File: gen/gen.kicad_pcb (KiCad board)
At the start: 2 copper layers, 40.6 x 40.6 mm, 16 parts

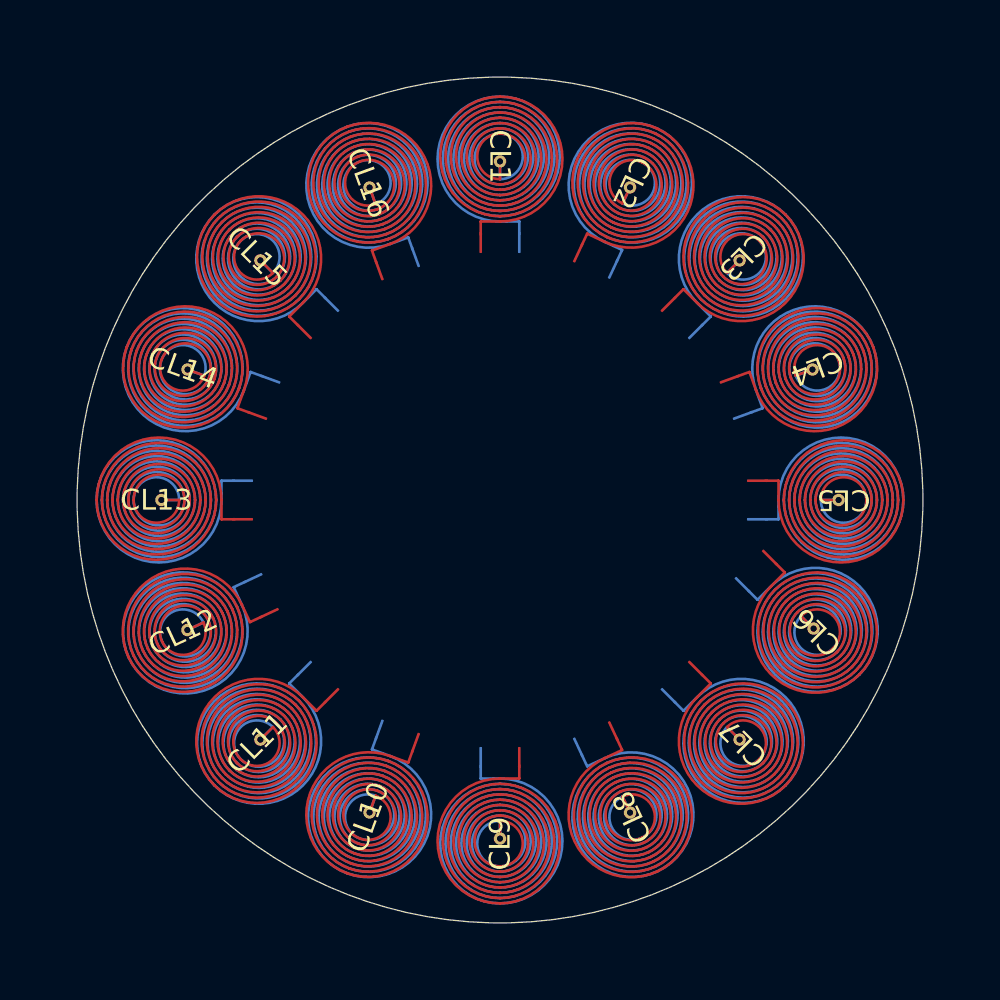
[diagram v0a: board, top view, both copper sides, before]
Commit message: Added 6 layer coils
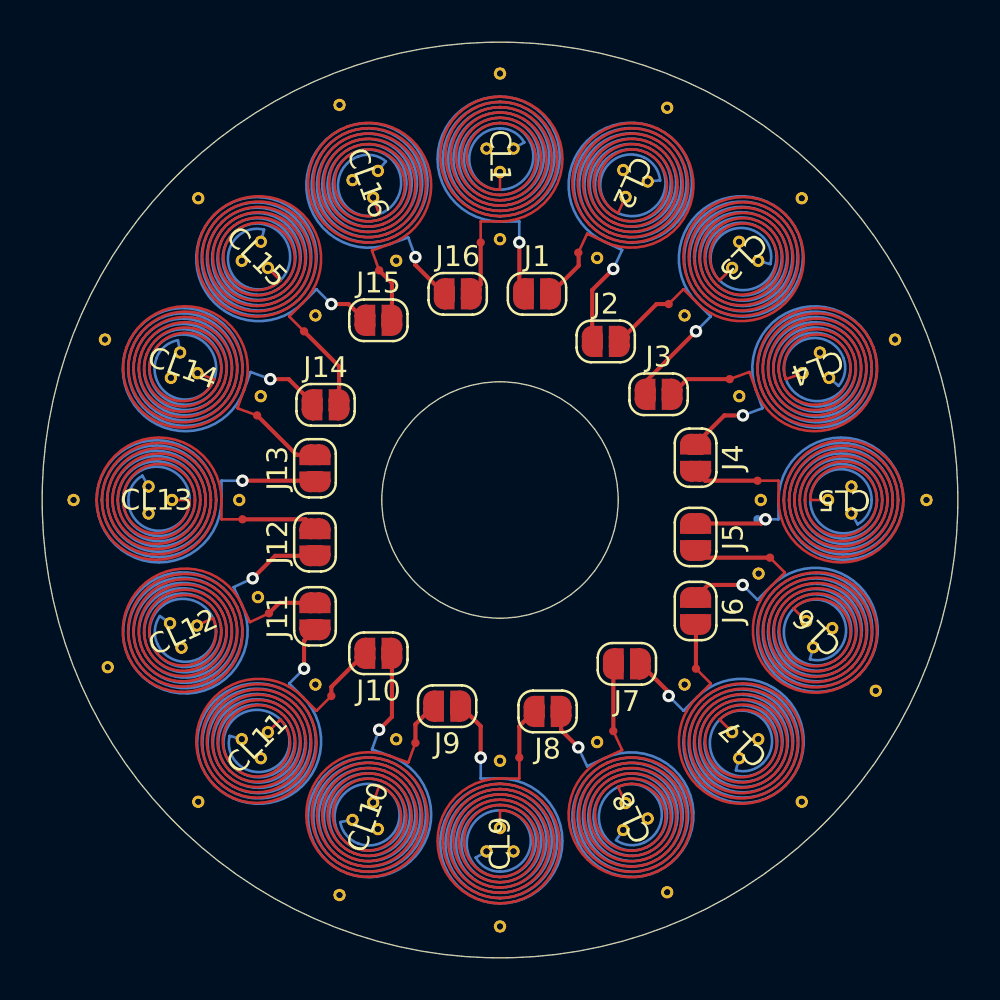
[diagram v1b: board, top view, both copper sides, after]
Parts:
- added J1: Conn_01x02_Pin, Jumper:SolderJumper-2_P1.3mm_Open_RoundedPad1.0x1.5mm, F.Cu at (154.2, 91.7)
- added J10: Conn_01x02_Pin, Jumper:SolderJumper-2_P1.3mm_Open_RoundedPad1.0x1.5mm, F.Cu at (146.6, 109.0)
- added J11: Conn_01x02_Pin, Jumper:SolderJumper-2_P1.3mm_Open_RoundedPad1.0x1.5mm, F.Cu at (143.5, 107.2)
- added J12: Conn_01x02_Pin, Jumper:SolderJumper-2_P1.3mm_Open_RoundedPad1.0x1.5mm, F.Cu at (143.5, 103.6)
- added J13: Conn_01x02_Pin, Jumper:SolderJumper-2_P1.3mm_Open_RoundedPad1.0x1.5mm, F.Cu at (143.5, 100.1)
- added J14: Conn_01x02_Pin, Jumper:SolderJumper-2_P1.3mm_Open_RoundedPad1.0x1.5mm, F.Cu at (144.0, 97.0)
- added J15: Conn_01x02_Pin, Jumper:SolderJumper-2_P1.3mm_Open_RoundedPad1.0x1.5mm, F.Cu at (146.6, 93.0)
- added J16: Conn_01x02_Pin, Jumper:SolderJumper-2_P1.3mm_Open_RoundedPad1.0x1.5mm, F.Cu at (150.4, 91.7)
- added J2: Conn_01x02_Pin, Jumper:SolderJumper-2_P1.3mm_Open_RoundedPad1.0x1.5mm, F.Cu at (157.5, 94.0)
- added J3: Conn_01x02_Pin, Jumper:SolderJumper-2_P1.3mm_Open_RoundedPad1.0x1.5mm, F.Cu at (160.0, 96.5)
- added J4: Conn_01x02_Pin, Jumper:SolderJumper-2_P1.3mm_Open_RoundedPad1.0x1.5mm, F.Cu at (161.8, 99.6)
- added J5: Conn_01x02_Pin, Jumper:SolderJumper-2_P1.3mm_Open_RoundedPad1.0x1.5mm, F.Cu at (161.8, 103.4)
- added J6: Conn_01x02_Pin, Jumper:SolderJumper-2_P1.3mm_Open_RoundedPad1.0x1.5mm, F.Cu at (161.8, 106.9)
- added J7: Conn_01x02_Pin, Jumper:SolderJumper-2_P1.3mm_Open_RoundedPad1.0x1.5mm, F.Cu at (158.5, 109.5)
- added J8: Conn_01x02_Pin, Jumper:SolderJumper-2_P1.3mm_Open_RoundedPad1.0x1.5mm, F.Cu at (154.7, 111.8)
- added J9: Conn_01x02_Pin, Jumper:SolderJumper-2_P1.3mm_Open_RoundedPad1.0x1.5mm, F.Cu at (149.9, 111.5)
- CL1, CL10, CL11, CL12, CL13, CL14, CL15, CL16, CL2, CL3, CL4, CL5, CL6, CL7, CL8, CL9: value SMALL_COIL -> L; footprint PCB Coils:SMALL_COIL -> PCB Coils:SMALL_COIL_6
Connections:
- CL1 pad 1: (no net) -> Net-(J16-Pin_2)
- CL1 pad 2: (no net) -> Net-(J1-Pin_1)
- CL10 pad 1: (no net) -> Net-(J9-Pin_2)
- CL10 pad 2: (no net) -> Net-(J10-Pin_1)
- CL11 pad 1: (no net) -> Net-(J10-Pin_2)
- CL11 pad 2: (no net) -> Net-(J11-Pin_1)
- CL12 pad 1: (no net) -> Net-(J11-Pin_2)
- CL12 pad 2: (no net) -> Net-(J12-Pin_1)
- CL13 pad 1: (no net) -> Net-(J12-Pin_2)
- CL13 pad 2: (no net) -> Net-(J13-Pin_1)
- CL14 pad 1: (no net) -> Net-(J13-Pin_2)
- CL14 pad 2: (no net) -> Net-(J14-Pin_1)
- CL15 pad 1: (no net) -> Net-(J14-Pin_2)
- CL15 pad 2: (no net) -> Net-(J15-Pin_1)
- CL16 pad 1: (no net) -> Net-(J15-Pin_2)
- CL16 pad 2: (no net) -> Net-(J16-Pin_1)
- CL2 pad 1: (no net) -> Net-(J1-Pin_2)
- CL2 pad 2: (no net) -> Net-(J2-Pin_1)
- CL3 pad 1: (no net) -> Net-(J2-Pin_2)
- CL3 pad 2: (no net) -> Net-(J3-Pin_1)
- CL4 pad 1: (no net) -> Net-(J3-Pin_2)
- CL4 pad 2: (no net) -> Net-(J4-Pin_1)
- CL5 pad 1: (no net) -> Net-(J4-Pin_2)
- CL5 pad 2: (no net) -> Net-(J5-Pin_1)
- CL6 pad 1: (no net) -> Net-(J5-Pin_2)
- CL6 pad 2: (no net) -> Net-(J6-Pin_1)
- CL7 pad 1: (no net) -> Net-(J6-Pin_2)
- CL7 pad 2: (no net) -> Net-(J7-Pin_1)
- CL8 pad 1: (no net) -> Net-(J7-Pin_2)
- CL8 pad 2: (no net) -> Net-(J8-Pin_1)
- CL9 pad 1: (no net) -> Net-(J8-Pin_2)
- CL9 pad 2: (no net) -> Net-(J9-Pin_1)
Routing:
- net Net-(J14-Pin_2): track 0.00 -> 4.23 mm
- net Net-(J3-Pin_1): track 0.00 -> 4.04 mm, vias 0 -> 1
- net Net-(J10-Pin_1): track 0.00 -> 3.93 mm, vias 0 -> 1
- net Net-(J2-Pin_1): track 0.00 -> 3.90 mm, vias 0 -> 1
- net Net-(J5-Pin_2): track 0.00 -> 3.72 mm
- net Net-(J12-Pin_2): track 0.00 -> 3.67 mm
- net Net-(J13-Pin_2): track 0.00 -> 3.56 mm
- net Net-(J13-Pin_1): track 0.00 -> 3.51 mm, vias 0 -> 1
- net Net-(J12-Pin_1): track 0.00 -> 3.44 mm, vias 0 -> 1
- net Net-(J5-Pin_1): track 0.00 -> 3.44 mm, vias 0 -> 1
- net Net-(J7-Pin_2): track 0.00 -> 3.23 mm
- net Net-(J4-Pin_2): track 0.00 -> 3.17 mm
- net Net-(J2-Pin_2): track 0.00 -> 3.12 mm
- net Net-(J3-Pin_2): track 0.00 -> 3.07 mm
- net Net-(J9-Pin_1): track 0.00 -> 2.87 mm, vias 0 -> 1
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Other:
- board size 40.6 x 40.6 mm -> 44 x 44 mm
- copper layers 2 -> 6
